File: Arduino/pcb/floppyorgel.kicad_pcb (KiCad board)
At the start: 2 copper layers, 50 x 50 mm, 36 parts, among them J1 VCC_Power_Select, J2 Floppy-Bus, J3 MAX485 Socket, J4 Floppy-Bus, J5 Buck-Converter-5V, J6 Buck-Converter-12V, J7 Floppy-Power, J8 IBM_PC_Floppy_IDC, J9 FTDI, SW1 Bus Address Select, SW2 Reset Button, U1 4021, U2 ATMEGA328P-AU, U3 24LC64, Y1 20 Mhz Crystal

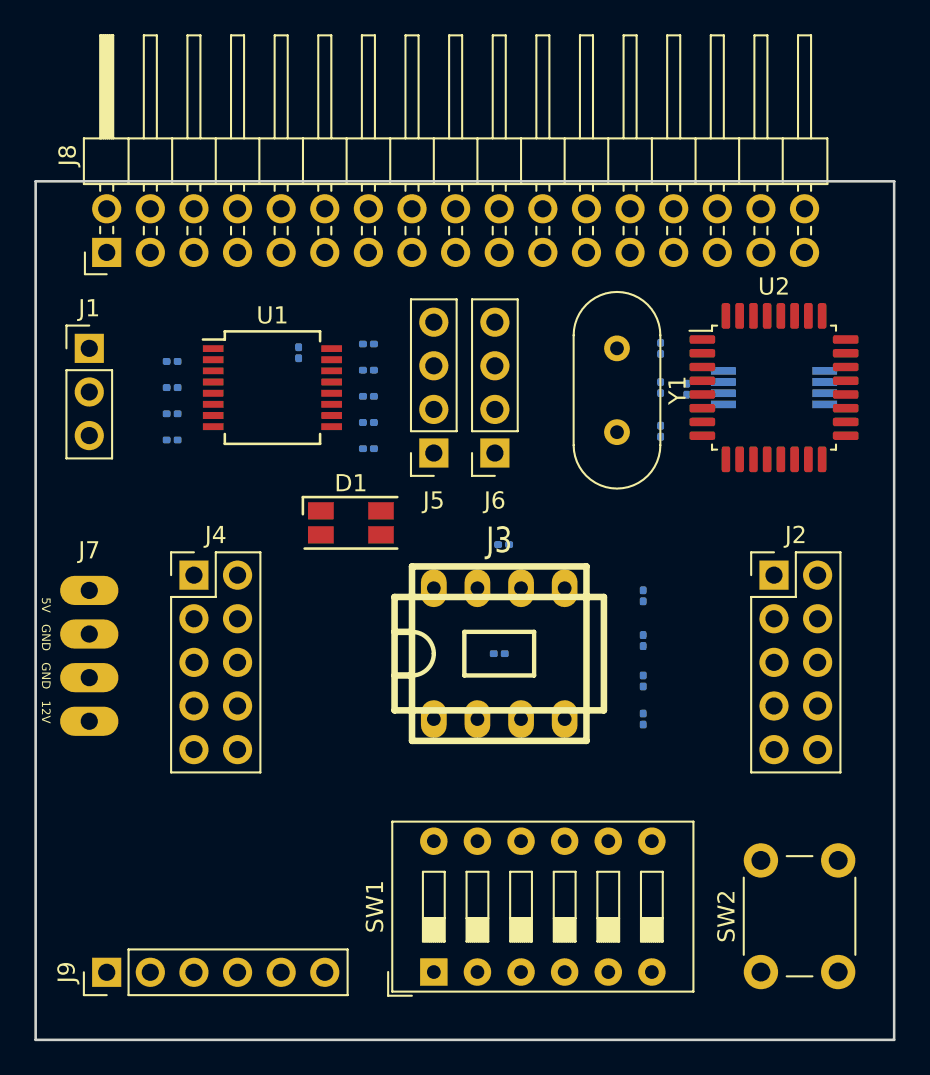
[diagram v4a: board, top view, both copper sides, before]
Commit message: pcb: continue placement + add some info on silk
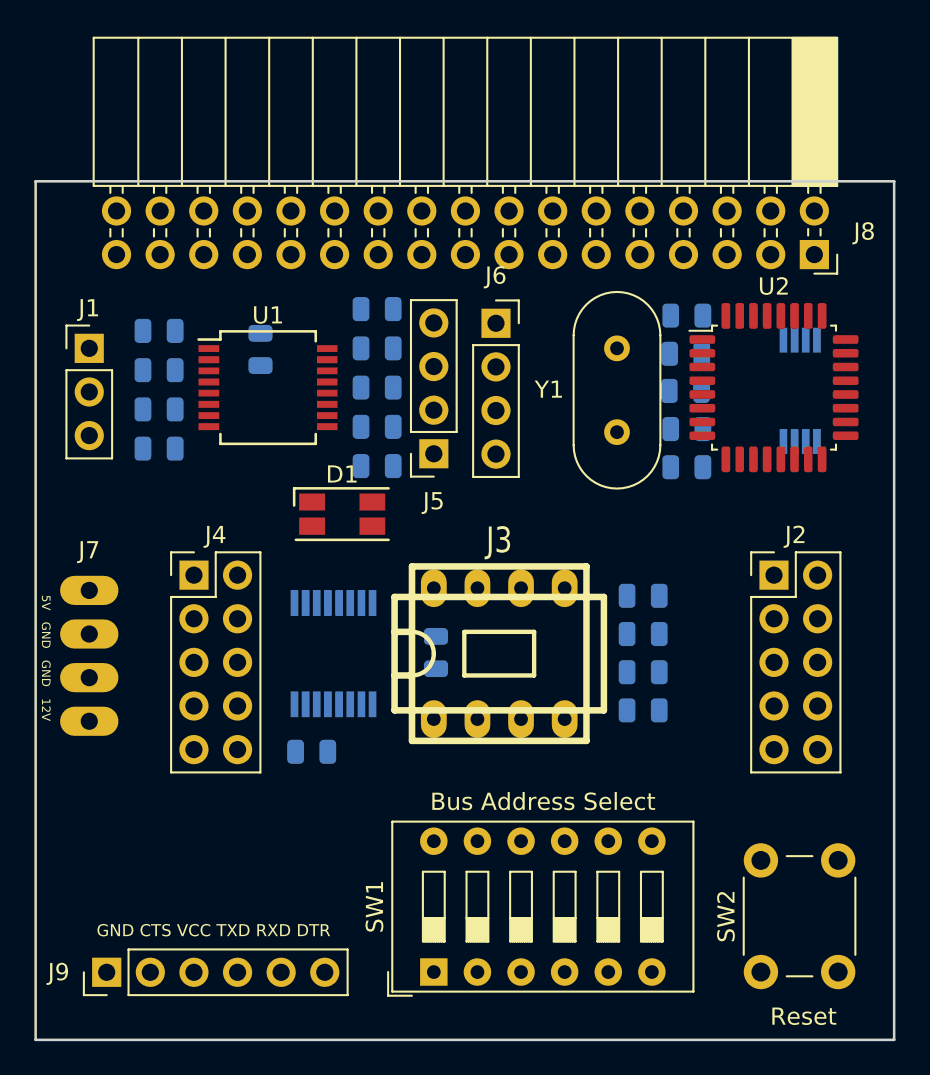
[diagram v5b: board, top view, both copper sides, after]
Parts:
- added C8: 100nF, Capacitor_SMD:C_0805_2012Metric, B.Cu at (116.1, 133.2)
- added U4: 74HC595, Package_SO:TSSOP-16_4.4x5mm_P0.65mm, B.Cu at (117.3, 127.5)
- C1, C2, C3, C5, C7: footprint Capacitor_SMD:C_0201_0603Metric -> Capacitor_SMD:C_0805_2012Metric
- C4: value 100nF -> 22pF; footprint Capacitor_SMD:C_0201_0603Metric -> Capacitor_SMD:C_0805_2012Metric
- C6: value 22pF -> 100nF; footprint Capacitor_SMD:C_0201_0603Metric -> Capacitor_SMD:C_0805_2012Metric
- D1: value WS2812B -> LED_RGB
- J8: footprint Connector_PinHeader_2.54mm:PinHeader_2x17_P2.54mm_Horizontal -> Connector_PinSocket_2.54mm:PinSocket_2x17_P2.54mm_Horizontal
- R1, R10, R11, R12, R13, R2, R3, R4, R5, R6, R7, R8, R9: footprint Capacitor_SMD:C_0201_0603Metric -> Resistor_SMD:R_0805_2012Metric
- moved J8 41.2 mm to (145.4, 104.3), turned to 270 degrees
- moved C7 23.6 mm to (137.9, 116.6), turned to 180 degrees
- moved C3 22.5 mm to (137.9, 107.8)
- moved C1 20.2 mm to (123.3, 127.4)
- moved C2 18.2 mm to (113.1, 109.8), turned to 270 degrees
- moved J6 7.56 mm to (126.8, 108.3), turned to 0 degrees
- moved C6 4.94 mm to (137.9, 114.4), turned to 0 degrees
- moved C5 2.76 mm to (137.8, 112.2), turned to 0 degrees
- moved R13 2.09 mm to (119.9, 107.4)
- moved C4 2.06 mm to (137.9, 110.0), turned to 180 degrees
- moved R3 1.93 mm to (107.2, 108.7)
- moved U3 1.54 mm to (144.5, 112.2), turned to 270 degrees
- moved R12 1.37 mm to (119.9, 109.7)
- moved R4 1.27 mm to (107.2, 111.0)
- moved R1 1.14 mm to (119.9, 116.6)
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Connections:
- C3 pad 1: VCC -> Net-(C3-Pad1)
- C3 pad 2: GND -> Net-(C3-Pad2)
- C4 pad 1: Net-(C4-Pad1) -> GND
- C5 pad 1: GND -> Net-(C5-Pad1)
- C5 pad 2: Net-(C5-Pad2) -> GND
- C6 pad 1: Net-(C6-Pad1) -> VCC
- D1 pad 1: VCC -> GND
- D1 pad 2: (no net) -> GND
- D1 pad 4: /MCU/DATA_LED -> Net-(D1-Pad4)
- J9 pad 6: Net-(C4-Pad2) -> Net-(C3-Pad2)
- R9 pad 2: Net-(C4-Pad1) -> Net-(C3-Pad1)
- SW2 pad 1: Net-(C4-Pad1) -> Net-(C3-Pad1)
- U2 pad 15: (no net) -> /Led/MOSI
- U2 pad 25: /MCU/DATA_LED -> /Led/LATCH_LED
- U2 pad 29: Net-(C4-Pad1) -> Net-(C3-Pad1)
- U2 pad 7: Net-(C5-Pad2) -> Net-(C4-Pad2)
- U2 pad 8: Net-(C6-Pad1) -> Net-(C5-Pad1)
- Y1 pad 1: Net-(C6-Pad1) -> Net-(C5-Pad1)
- Y1 pad 2: Net-(C5-Pad2) -> Net-(C4-Pad2)
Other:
- board text added: "Bus Address Select"
- board text added: "Floppy Module 3.0"
- board text added: "GND CTS VCC TXD RXD DTR"
- board text added: "Reset"
- board text added: "coon 04.05.2019"

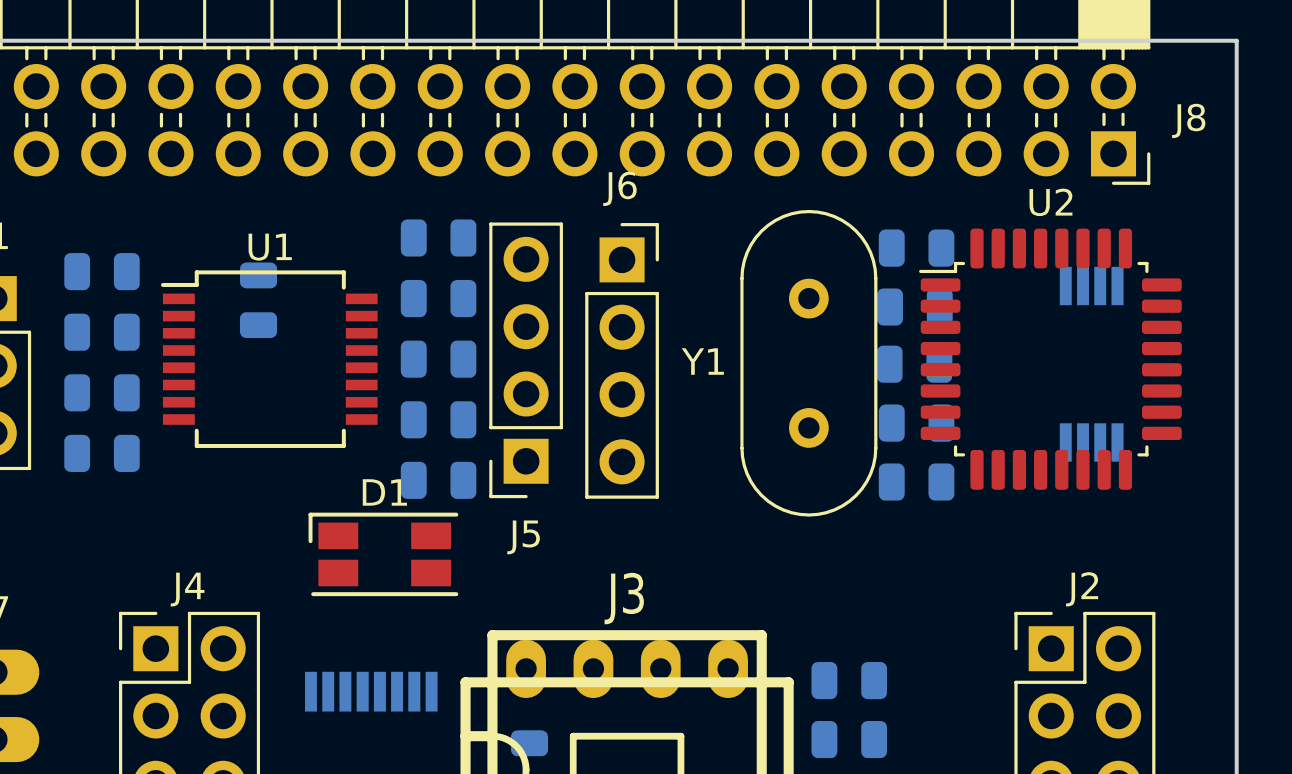
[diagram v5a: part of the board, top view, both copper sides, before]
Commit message: pcb: add testpads for SPI
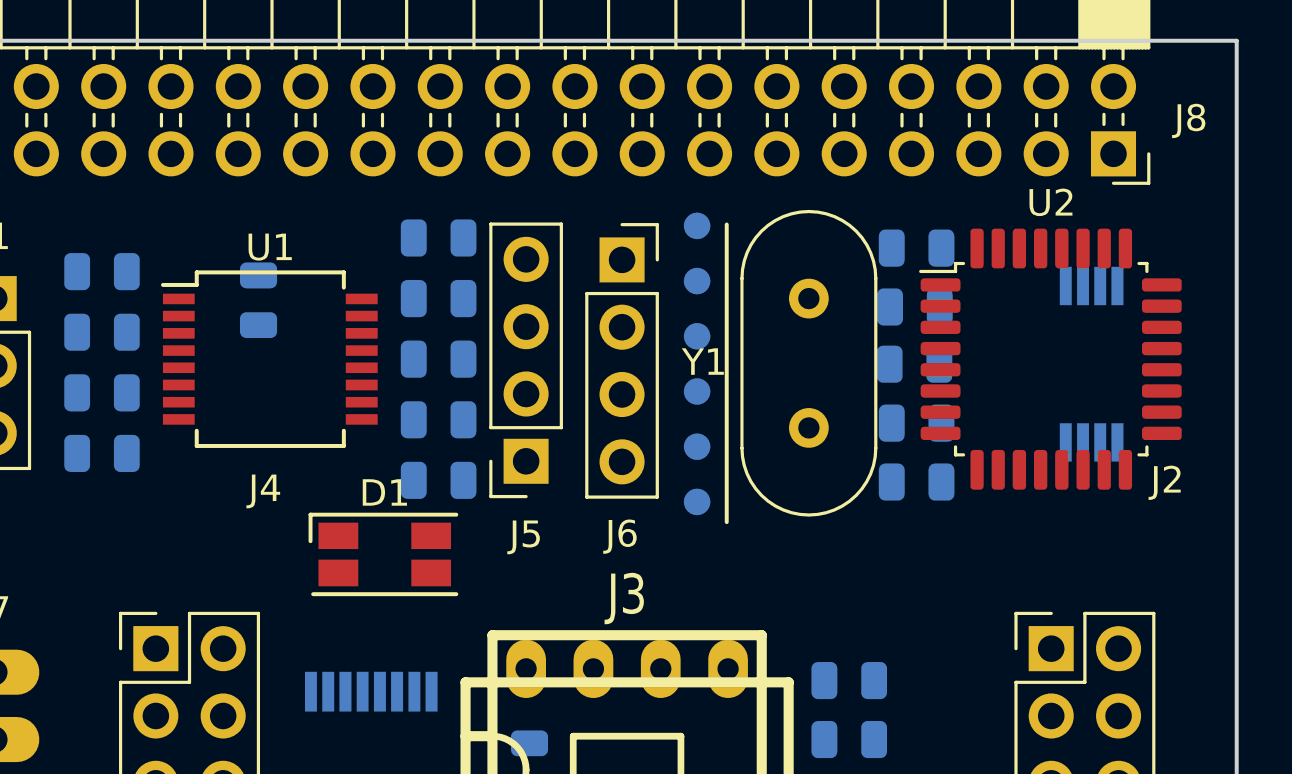
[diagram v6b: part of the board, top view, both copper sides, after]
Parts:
- added TP1: MISO, TestPoint:TestPoint_Pad_D1.0mm, B.Cu at (129.6, 107.0)
- added TP2: MOSI, TestPoint:TestPoint_Pad_D1.0mm, B.Cu at (129.6, 109.1)
- added TP3: SCK, TestPoint:TestPoint_Pad_D1.0mm, B.Cu at (129.6, 111.2)
- added TP4: RESET, TestPoint:TestPoint_Pad_D1.0mm, B.Cu at (129.6, 113.2)
- added TP5: VCC, TestPoint:TestPoint_Pad_D1.0mm, B.Cu at (129.6, 115.3)
- added TP6: GND, TestPoint:TestPoint_Pad_D1.0mm, B.Cu at (129.6, 117.4)
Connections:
- net Net-(C3-Pad1) renamed /MCU/RESET
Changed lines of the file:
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@@
   (general
     (thickness 1.6)
-    (drawings 12)
+    (drawings 13)
     (tracks 0)
     (zones 0)
-    (modules 38)
+    (modules 44)
     (nets 40)
   )
@@
   (net 36 /Led/LATCH_LED)
   (net 37 "Net-(C3-Pad2)")
-  (net 38 "Net-(C3-Pad1)")
-  (net 39 "Net-(C5-Pad1)")
+  (net 38 "Net-(C5-Pad1)")
+  (net 39 /MCU/RESET)
   (net_class Default "This is the default net class."
     (clearance 0.2)
@@
     (add_net /Led/LATCH_LED)
     (add_net /Led/MOSI)
+    (add_net /MCU/RESET)
     (add_net /MCU/RX)
     (add_net /MCU/SCL)
     (add_net /MCU/SDA)
     (add_net GND)
-    (add_net "Net-(C3-Pad1)")
     (add_net "Net-(C3-Pad2)")
     (add_net "Net-(C4-Pad2)")
@@
     (descr "Through hole straight pin header, 2x05, 2.54mm pitch, double rows")
     (tags "Through hole pin header THT 2x05 2.54mm double row")
-    (fp_text reference J2 (at 1.27 -2.33 180) (layer F.SilkS)
+    (fp_text reference J2 (at 4.3815 -6.35 180) (layer F.SilkS)
       (effects (font (size 1 1) (thickness 0.15)))
     )
@@
     (descr "Through hole straight pin header, 2x05, 2.54mm pitch, double rows")
     (tags "Through hole pin header THT 2x05 2.54mm double row")
-    (fp_text reference J4 (at 1.27 -2.33) (layer F.SilkS)
+    (fp_text reference J4 (at 4.1275 -6.0325) (layer F.SilkS)
       (effects (font (size 1 1) (thickness 0.15)))
     )
@@
     (descr "Through hole straight socket strip, 1x04, 2.54mm pitch, single row (from Kicad 4.0.7), script generated")
     (tags "Through hole socket strip THT 1x04 2.54mm single row")
-    (fp_text reference J6 (at 0 -2.77) (layer F.SilkS)
+    (fp_text reference J6 (at 0 10.3505) (layer F.SilkS)
       (effects (font (size 1 1) (thickness 0.15)))
     )
@@
       (net 27 "Net-(R10-Pad1)"))
     (pad 1 thru_hole circle (at 0 0 180) (size 2 2) (drill 1.1) (layers *.Cu *.Mask)
-      (net 38 "Net-(C3-Pad1)"))
+      (net 39 /MCU/RESET))
     (pad 2 thru_hole circle (at 6.5 4.5 180) (size 2 2) (drill 1.1) (layers *.Cu *.Mask)
       (net 27 "Net-(R10-Pad1)"))
     (pad 1 thru_hole circle (at 6.5 0 180) (size 2 2) (drill 1.1) (layers *.Cu *.Mask)
-      (net 38 "Net-(C3-Pad1)"))
+      (net 39 /MCU/RESET))
     (model ${KISYS3DMOD}/Button_Switch_THT.3dshapes/SW_PUSH_6mm.wrl
       (at (xyz 0 0 0))
@@
       (net 31 "Net-(C4-Pad2)"))
     (pad 8 smd roundrect (at -4.175 2.8) (size 1.5 0.5) (layers F.Cu F.Paste F.Mask) (roundrect_rratio 0.25)
-      (net 39 "Net-(C5-Pad1)"))
+      (net 38 "Net-(C5-Pad1)"))
     (pad 9 smd roundrect (at -2.8 4.175) (size 0.5 1.5) (layers F.Cu F.Paste F.Mask) (roundrect_rratio 0.25))
     (pad 10 smd roundrect (at -2 4.175) (size 0.5 1.5) (layers F.Cu F.Paste F.Mask) (roundrect_rratio 0.25))
@@
       (net 33 /MCU/SCL))
     (pad 29 smd roundrect (at -0.4 -4.175) (size 0.5 1.5) (layers F.Cu F.Paste F.Mask) (roundrect_rratio 0.25)
-      (net 38 "Net-(C3-Pad1)"))
+      (net 39 /MCU/RESET))
     (pad 30 smd roundrect (at -1.2 -4.175) (size 0.5 1.5) (layers F.Cu F.Paste F.Mask) (roundrect_rratio 0.25)
       (net 7 "Net-(J9-Pad4)"))
@@
     (fp_arc (start 5.64 0) (end 5.64 -2.525) (angle 180) (layer F.SilkS) (width 0.12))
     (pad 1 thru_hole circle (at 0 0 270) (size 1.5 1.5) (drill 0.8) (layers *.Cu *.Mask)
-      (net 39 "Net-(C5-Pad1)"))
+      (net 38 "Net-(C5-Pad1)"))
     (pad 2 thru_hole circle (at 4.88 0 270) (size 1.5 1.5) (drill 0.8) (layers *.Cu *.Mask)
       (net 31 "Net-(C4-Pad2)"))
@@
       (net 37 "Net-(C3-Pad2)"))
     (pad 1 smd roundrect (at -0.9375 0) (size 0.975 1.4) (layers B.Cu B.Paste B.Mask) (roundrect_rratio 0.25)
-      (net 38 "Net-(C3-Pad1)"))
+      (net 39 /MCU/RESET))
     (model ${KISYS3DMOD}/Capacitor_SMD.3dshapes/C_0805_2012Metric.wrl
       (at (xyz 0 0 0))
@@
       (net 9 GND))
     (pad 1 smd roundrect (at -0.9375 0) (size 0.975 1.4) (layers B.Cu B.Paste B.Mask) (roundrect_rratio 0.25)
-      (net 39 "Net-(C5-Pad1)"))
+      (net 38 "Net-(C5-Pad1)"))
     (model ${KISYS3DMOD}/Capacitor_SMD.3dshapes/C_0805_2012Metric.wrl
       (at (xyz 0 0 0))
@@
       (net 8 VCC))
     (pad 2 smd roundrect (at 0.9375 0) (size 0.975 1.4) (layers B.Cu B.Paste B.Mask) (roundrect_rratio 0.25)
-      (net 38 "Net-(C3-Pad1)"))
+      (net 39 /MCU/RESET))
     (model ${KISYS3DMOD}/Resistor_SMD.3dshapes/R_0805_2012Metric.wrl
       (at (xyz 0 0 0))
@@
     )
   )
+  (module TestPoint:TestPoint_Pad_D1.0mm (layer B.Cu)
+    (at 129.6416 106.9848)
+    (descr "SMD pad as test Point, diameter 1.0mm")
+    (tags "test point SMD pad")
+    (attr virtual)
+    (fp_text reference TP1 (at 0 1.448) (layer B.SilkS) hide
+      (effects (font (size 1 1) (thickness 0.15)) (justify mirror))
+    )
+    (fp_text value MISO (at 1.9304 0) (layer B.SilkS)
+      (effects (font (size 0.5 0.5) (thickness 0.125)) (justify mirror))
+    )
+    (fp_circle (center 0 0) (end 1 0) (layer B.CrtYd) (width 0.05))
+    (fp_circle (center 0 0) (end 0 -0.7) (layer B.SilkS) (width 0.12))
+    (pad 1 smd circle (at 0 0) (size 1 1) (layers B.Cu B.Mask)
+      (net 29 /Floppy/MISO))
+  )
+  (module TestPoint:TestPoint_Pad_D1.0mm (layer B.Cu)
+    (at 129.6416 109.0676)
+    (descr "SMD pad as test Point, diameter 1.0mm")
+    (tags "test point SMD pad")
+    (attr virtual)
+    (fp_text reference TP2 (at 0 1.448) (layer B.SilkS) hide
+      (effects (font (size 1 1) (thickness 0.15)) (justify mirror))
+    )
+    (fp_text value MOSI (at 1.9304 0) (layer B.SilkS)
+      (effects (font (size 0.5 0.5) (thickness 0.125)) (justify mirror))
+    )
+    (fp_circle (center 0 0) (end 0 -0.7) (layer B.SilkS) (width 0.12))
+    (fp_circle (center 0 0) (end 1 0) (layer B.CrtYd) (width 0.05))
+    (pad 1 smd circle (at 0 0) (size 1 1) (layers B.Cu B.Mask)
+      (net 35 /Led/MOSI))
+  )
+  (module TestPoint:TestPoint_Pad_D1.0mm (layer B.Cu)
+    (at 129.6416 111.1504)
+    (descr "SMD pad as test Point, diameter 1.0mm")
+    (tags "test point SMD pad")
+    (attr virtual)
+    (fp_text reference TP3 (at 0 1.448) (layer B.SilkS) hide
+      (effects (font (size 1 1) (thickness 0.15)) (justify mirror))
+    )
+    (fp_text value SCK (at 1.778 0) (layer B.SilkS)
+      (effects (font (size 0.5 0.5) (thickness 0.125)) (justify mirror))
+    )
+    (fp_circle (center 0 0) (end 0 -0.7) (layer B.SilkS) (width 0.12))
+    (fp_circle (center 0 0) (end 1 0) (layer B.CrtYd) (width 0.05))
+    (pad 1 smd circle (at 0 0) (size 1 1) (layers B.Cu B.Mask)
+      (net 30 /Floppy/SCK))
+  )
+  (module TestPoint:TestPoint_Pad_D1.0mm (layer B.Cu)
+    (at 129.6416 113.2332)
+    (descr "SMD pad as test Point, diameter 1.0mm")
+    (tags "test point SMD pad")
+    (attr virtual)
+    (fp_text reference TP4 (at 0 1.448) (layer B.SilkS) hide
+      (effects (font (size 1 1) (thickness 0.15)) (justify mirror))
+    )
+    (fp_text value RESET (at 2.0828 0) (layer B.SilkS)
+      (effects (font (size 0.5 0.5) (thickness 0.125)) (justify mirror))
+    )
+    (fp_circle (center 0 0) (end 1 0) (layer B.CrtYd) (width 0.05))
+    (fp_circle (center 0 0) (end 0 -0.7) (layer B.SilkS) (width 0.12))
+    (pad 1 smd circle (at 0 0) (size 1 1) (layers B.Cu B.Mask)
+      (net 39 /MCU/RESET))
+  )
+  (module TestPoint:TestPoint_Pad_D1.0mm (layer B.Cu)
+    (at 129.6416 115.316)
+    (descr "SMD pad as test Point, diameter 1.0mm")
+    (tags "test point SMD pad")
+    (attr virtual)
+    (fp_text reference TP5 (at 0 1.448) (layer B.SilkS) hide
+      (effects (font (size 1 1) (thickness 0.15)) (justify mirror))
+    )
+    (fp_text value VCC (at 1.7272 0) (layer B.SilkS)
+      (effects (font (size 0.5 0.5) (thickness 0.125)) (justify mirror))
+    )
+    (fp_circle (center 0 0) (end 1 0) (layer B.CrtYd) (width 0.05))
+    (fp_circle (center 0 0) (end 0 -0.7) (layer B.SilkS) (width 0.12))
+    (pad 1 smd circle (at 0 0) (size 1 1) (layers B.Cu B.Mask)
+      (net 8 VCC))
+  )
+  (module TestPoint:TestPoint_Pad_D1.0mm (layer B.Cu)
+    (at 129.6416 117.3988)
+    (descr "SMD pad as test Point, diameter 1.0mm")
+    (tags "test point SMD pad")
+    (attr virtual)
+    (fp_text reference TP6 (at 0 1.448) (layer B.SilkS) hide
+      (effects (font (size 1 1) (thickness 0.15)) (justify mirror))
+    )
+    (fp_text value GND (at 1.8288 0) (layer B.SilkS)
+      (effects (font (size 0.5 0.5) (thickness 0.125)) (justify mirror))
+    )
+    (fp_circle (center 0 0) (end 0 -0.7) (layer B.SilkS) (width 0.12))
+    (fp_circle (center 0 0) (end 1 0) (layer B.CrtYd) (width 0.05))
+    (pad 1 smd circle (at 0 0) (size 1 1) (layers B.Cu B.Mask)
+      (net 9 GND))
+  )
+  (gr_line (start 130.7592 106.934) (end 130.7592 118.1608) (layer F.SilkS) (width 0.15))
   (gr_text Reset (at 144.7165 148.6535) (layer F.SilkS)
     (effects (font (size 1 1) (thickness 0.15)))
@@
     (effects (font (size 1.5 1.5) (thickness 0.3)) (justify mirror))
   )
-  (gr_text "coon 04.05.2019" (at 110.744 143.5735) (layer B.SilkS)
+  (gr_text "coon 04.05.2019" (at 110.49 148.463) (layer B.SilkS)
     (effects (font (size 1 1) (thickness 0.15)) (justify mirror))
   )
